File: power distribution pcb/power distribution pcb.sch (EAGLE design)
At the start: 30 parts, among them IC1 SN75176ASOIC, IC2 SN75176ASOIC, IC3 SN75176ASOIC, IC4 SN75176ASOIC, IC5 SN75176ASOIC, IC6 SN75176ASOIC

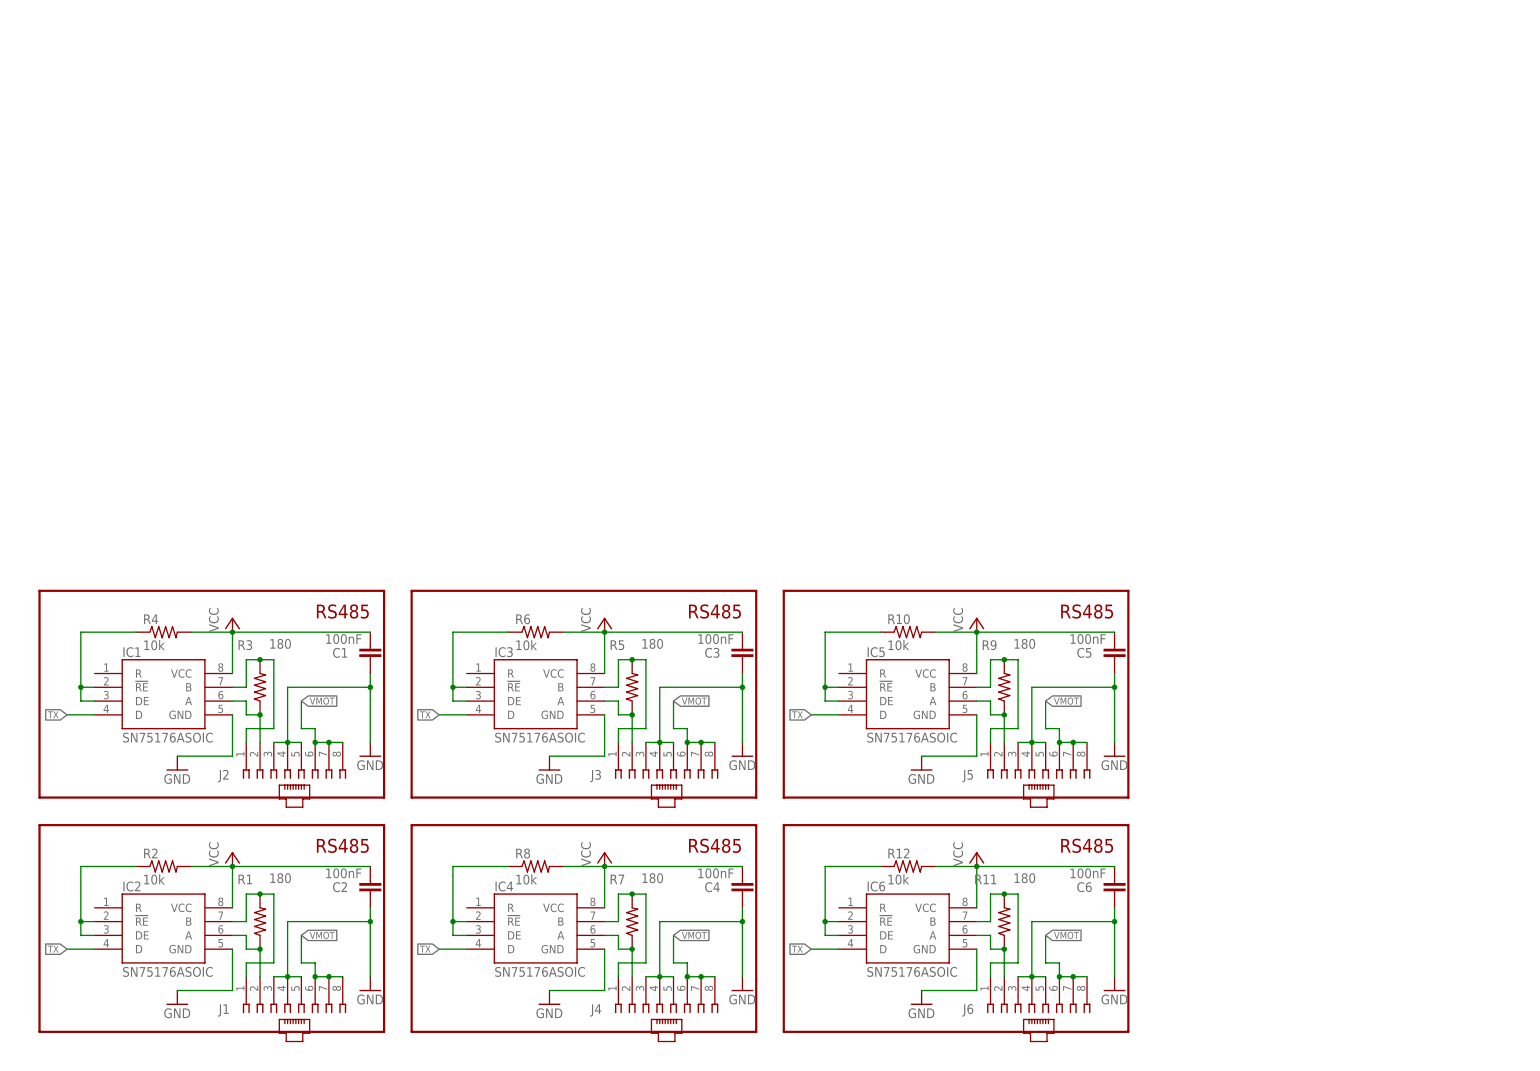
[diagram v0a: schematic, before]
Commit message: Add design files for power distribution board
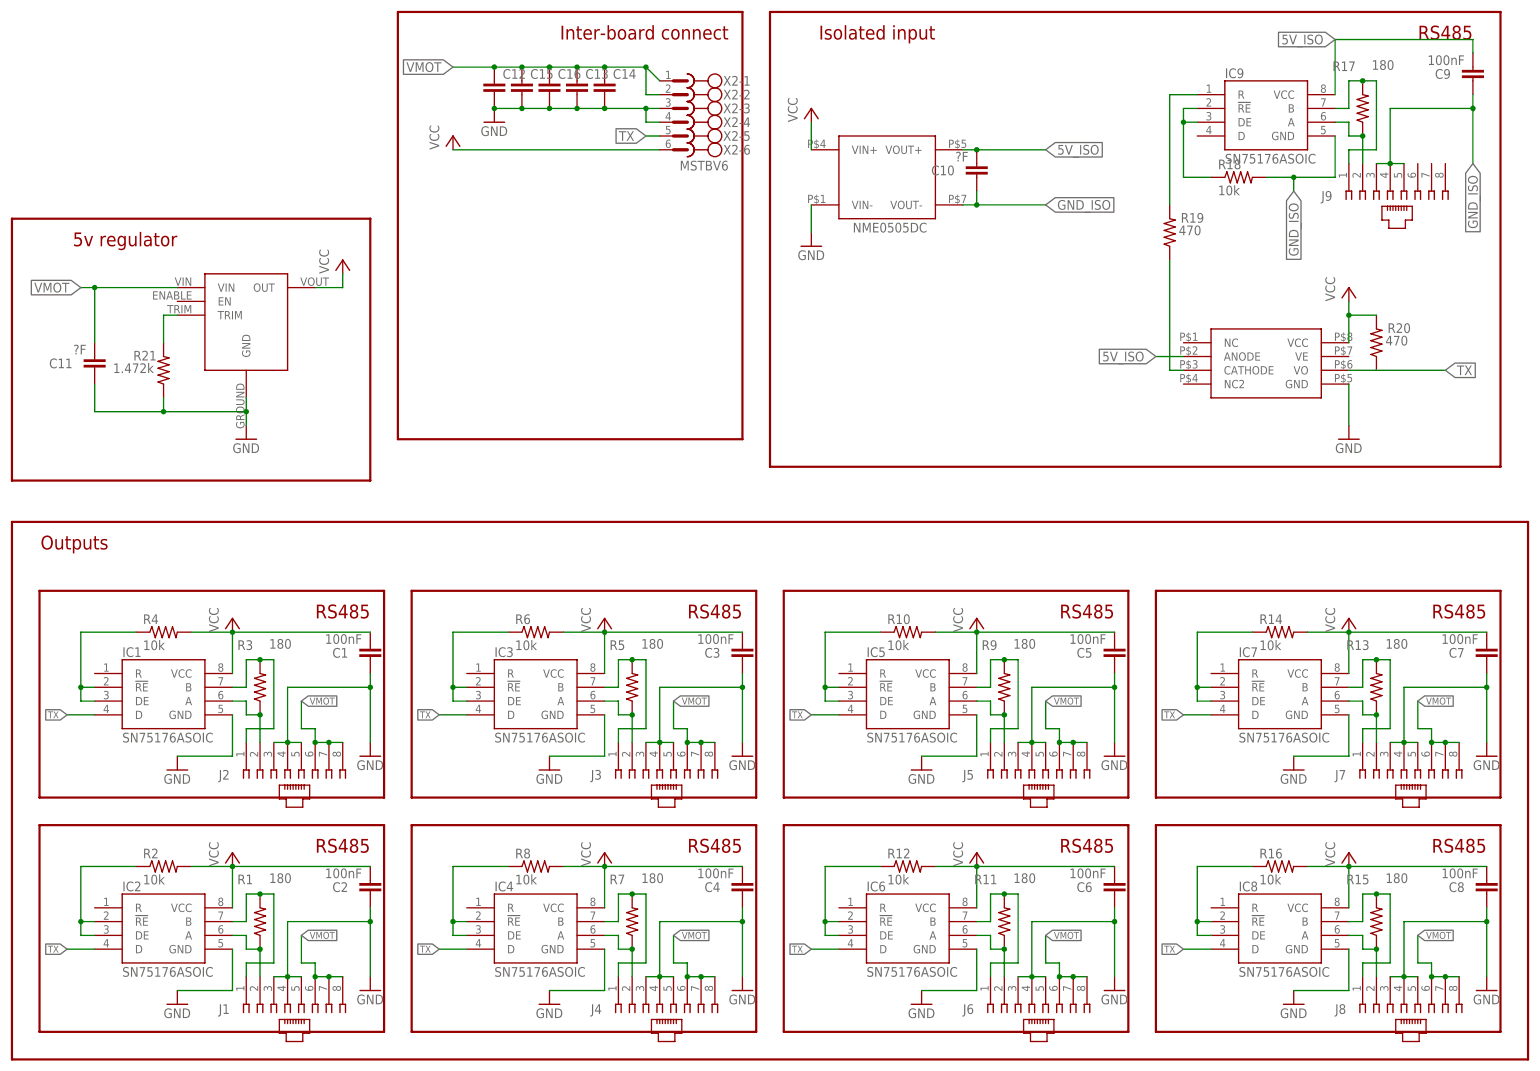
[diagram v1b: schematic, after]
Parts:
- added C10, C11: ?F, SparkFun:CAP0805
- added C12, C13, C14, C15, C16: (no value), SparkFun:CAP1210
- added C7, C8, C9: 100nF, SparkFun:CAP0805
- added IC7, IC8, IC9: SN75176ASOIC, reprap:SN75176ASOIC
- added J7, J8, J9: (no value), con-amp:520426-4
- added R13, R15, R17: 180, SparkFun:RESISTOR
- added R14, R16, R18: 10k, SparkFun:RESISTOR
- added R19, R20: 470, SparkFun:RESISTOR
- added R21: 1.472k, SparkFun:RESISTOR
- added U$1: NME0505DC, sonos_library:NME0505DC
- added U$2: OKI-T/3-W40N-C, sonos_library:OKI-T/3-W40N-C
- added U$3: 6N137, sonos_library:6N137
- added X2: MSTBV6, con-phoenix-508:MSTBV6
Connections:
- new net 5V_ISO: C10.2, C9.2, IC9.VCC, U$1.VOUT+, U$3.ANODE
- new net D7: IC7.!RE, IC7.DE, R14.1
- new net D8: IC8.!RE, IC8.DE, R16.1
- new net D9: IC9.!RE, IC9.DE, R18.1
- new net GND_ISO: C10.1, C9.1, IC9.GND, J9.3, J9.4, J9.5, R18.2, U$1.VOUT-
- new net N$1: R19.1, U$3.CATHODE
- new net N$3: IC9.R, R19.2
- new net N$9: R21.2, U$2.TRIM
- new net RS485A7: IC7.A, J7.2, R13.1
- new net RS485A8: IC8.A, J8.2, R15.1
- new net RS485A9: IC9.A, J9.2, R17.1
- new net RS485B7: IC7.B, J7.1, R13.2
- new net RS485B8: IC8.B, J8.1, R15.2
- new net RS485B9: IC9.B, J9.1, R17.2
- net GND: now also C11.1, C12.2, C13.2, C14.2, C15.2, C16.2, C7.1, C8.1, IC7.GND, IC8.GND, J7.3, J7.4, J7.5, J8.3, J8.4, J8.5, R21.1, U$1.VIN-, U$2.GND, U$3.GND, X2-3.1, X2-4.1
- net TX: now also IC7.D, IC8.D, R20.1, U$3.VO, X2-5.1
- net VCC: now also C7.2, C8.2, IC7.VCC, IC8.VCC, R14.2, R16.2, R20.2, U$1.VIN+, U$2.OUT, U$3.VCC, X2-6.1
- net VMOT: now also C11.2, C12.1, C13.1, C14.1, C15.1, C16.1, J7.6, J7.7, J7.8, J8.6, J8.7, J8.8, U$2.VIN, X2-1.1, X2-2.1
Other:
- note added: "5v regulator"
- note added: "Inter-board connect"
- note added: "Isolated input"
- note added: "Outputs"
